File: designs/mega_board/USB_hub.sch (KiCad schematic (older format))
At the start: 0 parts

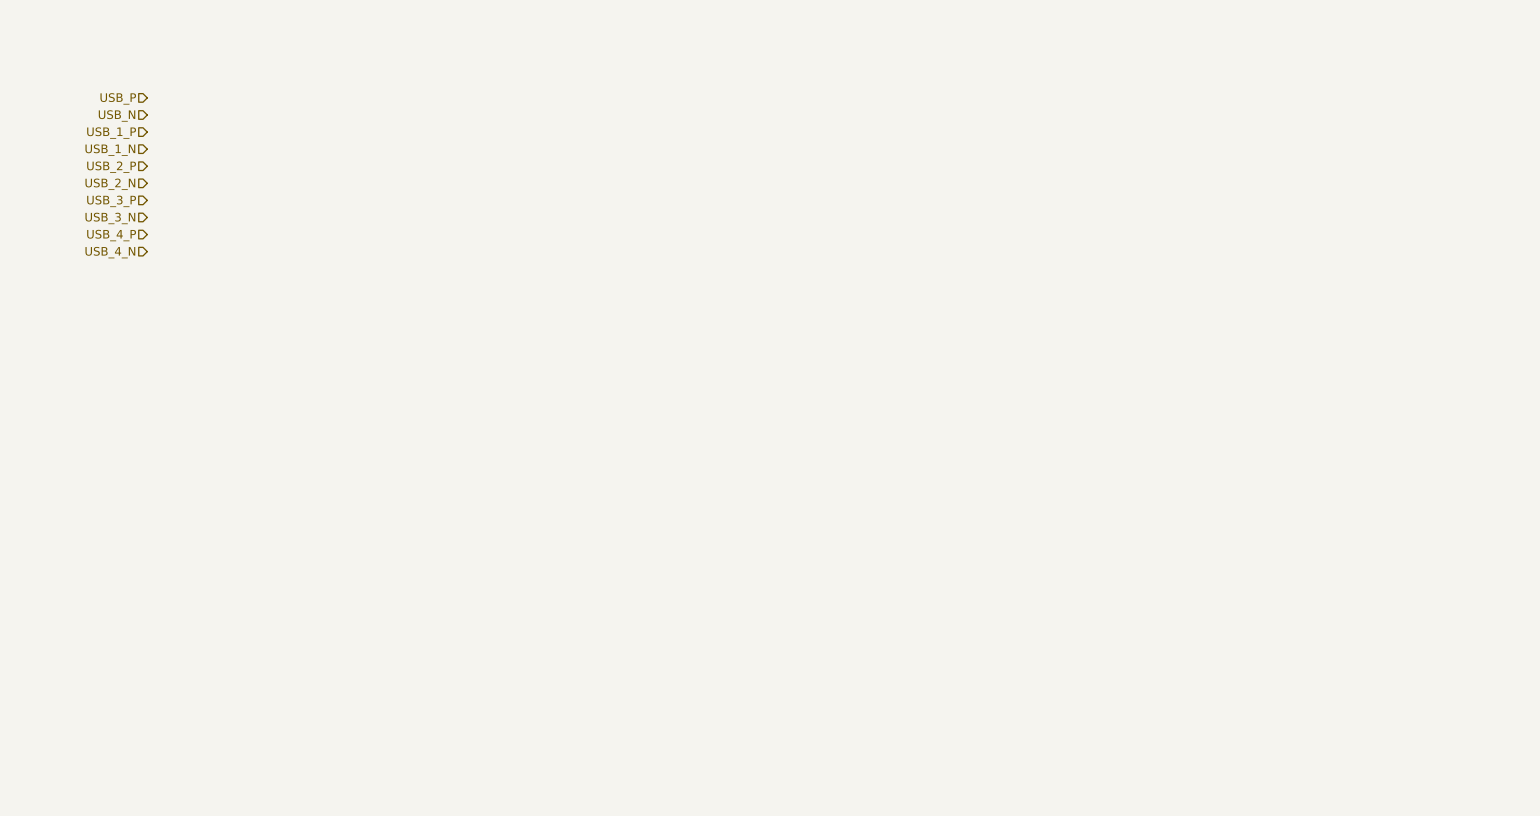
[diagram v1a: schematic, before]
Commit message: Complete usb sheet
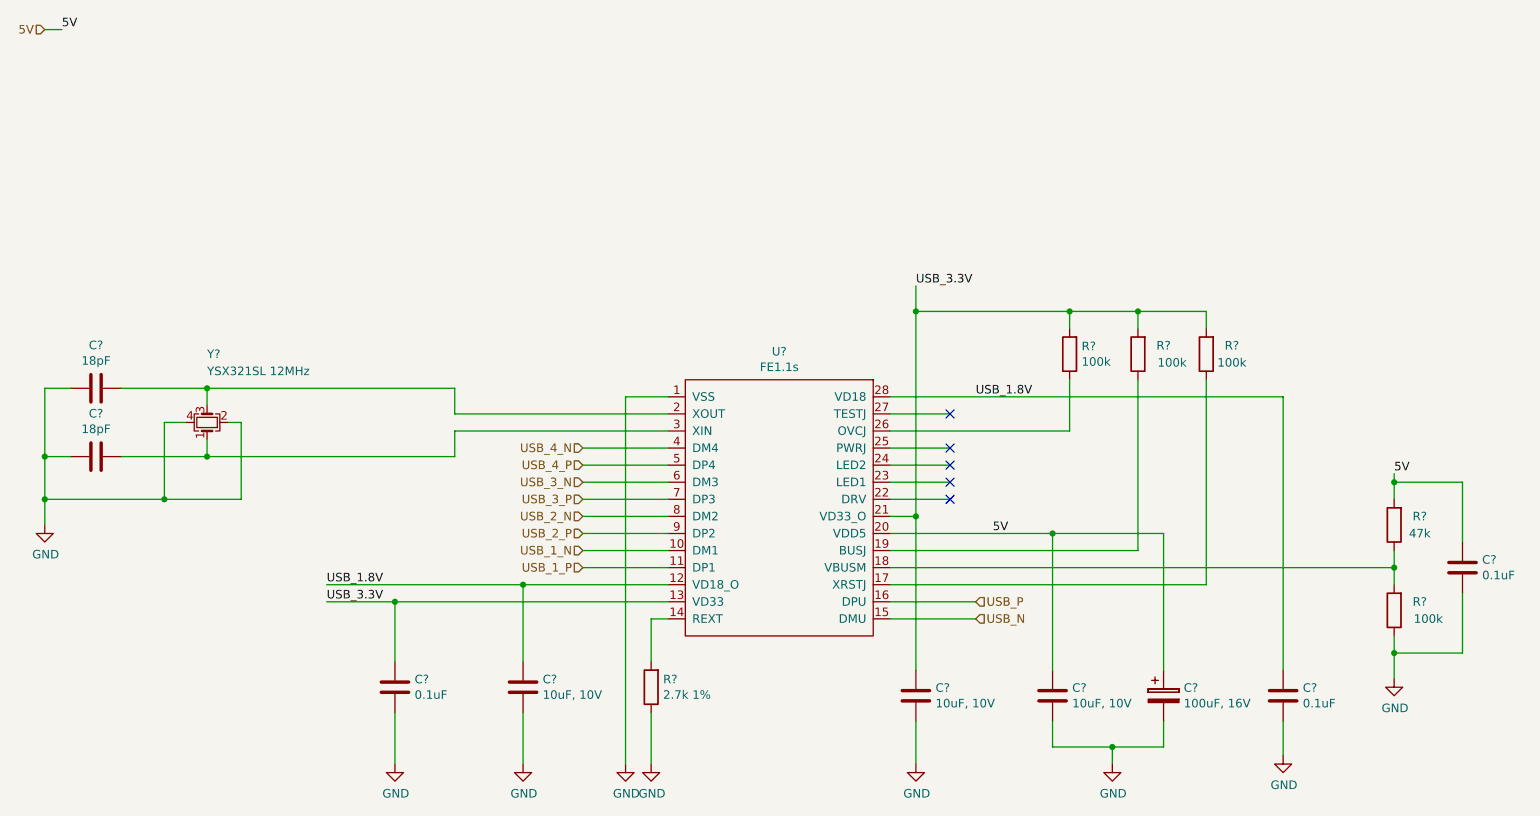
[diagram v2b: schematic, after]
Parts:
- added C? (x3): 10uF, 10V, symbol Device:C
- added C? (x3): 0.1uF, symbol Device:C
- added C?: 100uF, 16V, symbol Device:CP
- added C? (x2): 18pF, symbol Device:C
- added R? (x4): 100k, symbol Device:R
- added R?: 47k, symbol Device:R
- added R?: 2.7k 1%, symbol Device:R
- added U?: FE1.1s, symbol USB_HUB_FE1_1s:FE1.1s
- added Y?: YSX321SL 12MHz, symbol Device:Crystal_GND24_Small
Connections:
- net USB_1_N: now also U?.10 (DM1)
- net USB_1_P: now also U?.11 (DP1)
- net USB_2_N: now also U?.8 (DM2)
- net USB_2_P: now also U?.9 (DP2)
- net USB_3_N: now also U?.6 (DM3)
- net USB_3_P: now also U?.7 (DP3)
- net USB_4_N: now also U?.4 (DM4)
- net USB_4_P: now also U?.5 (DP4)
- net USB_N: now also U?.15 (DMU)
- net USB_P: now also U?.16 (DPU)
- new net: R?.2, U?.14 (REXT)
- new net: R?.1, U?.17 (XRSTJ)
- new net: R?.1, R?.2, U?.18 (VBUSM)
- new net: R?.1, U?.19 (BUSJ)
- new net: C?.1, U?.2 (XOUT), Y?.3
- new net: R?.1, U?.26 (OVCJ)
- new net: C?.1, U?.3 (XIN), Y?.1
- new net 5V: C?.1, C?.1, C?.1, R?.2, U?.20 (VDD5)
- new net GND: C?.2, C?.2, C?.2, C?.2, C?.2, C?.2, C?.2, C?.2, C?.2, R?.1, R?.1, U?.1 (VSS), Y?.2, Y?.4
- new net USB_1.8V: C?.1, C?.1, U?.12 (VD18_O), U?.28 (VD18)
- new net USB_3.3V: C?.1, C?.1, R?.2, R?.2, R?.2, U?.13 (VD33), U?.21 (VD33_O)
- no-connect marks 0 -> 5
